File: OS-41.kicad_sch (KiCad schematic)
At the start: 65 parts, among them J1 Conn_02x03_Counter_Clockwise, J2 Conn_01x02_Pin, J3 Conn_01x02_Pin, J4 Conn_Coaxial, SW4 SW_Push, U1 BME280, U2 SI4432-B1-FMR, U3 MCP1640x-xCHY, U4 ATGM336H-5N31, U7 STM32F103C8Tx, Y1 32.768KHz 12.5pF, Y2 8MHz 12pF, Y3 30MHz 10pF

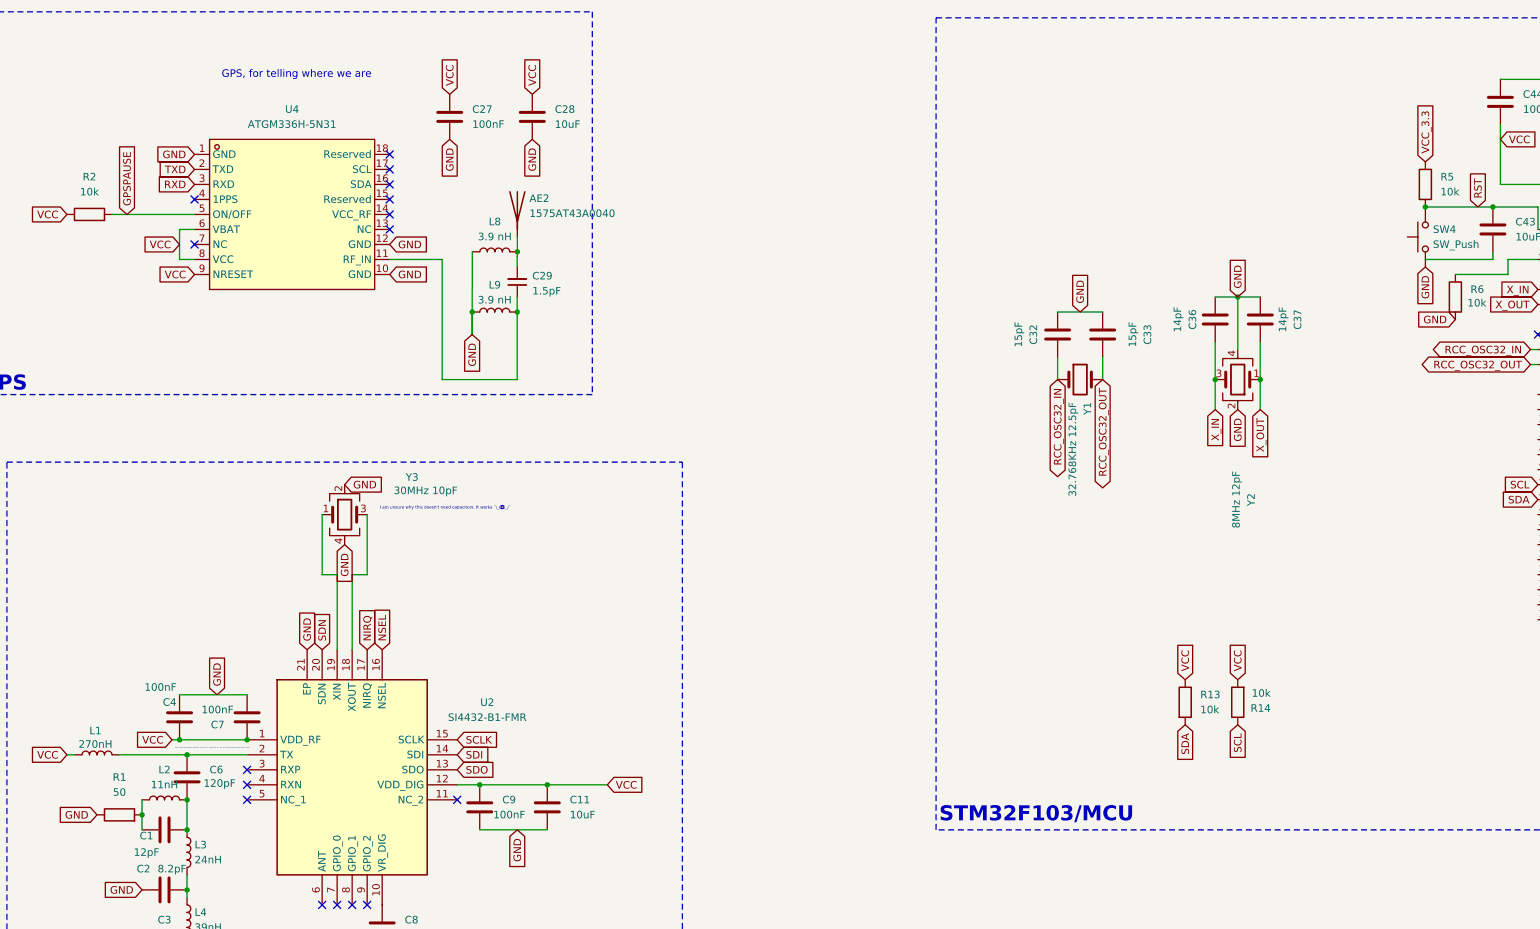
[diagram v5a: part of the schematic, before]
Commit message: More layout, no routing yet...
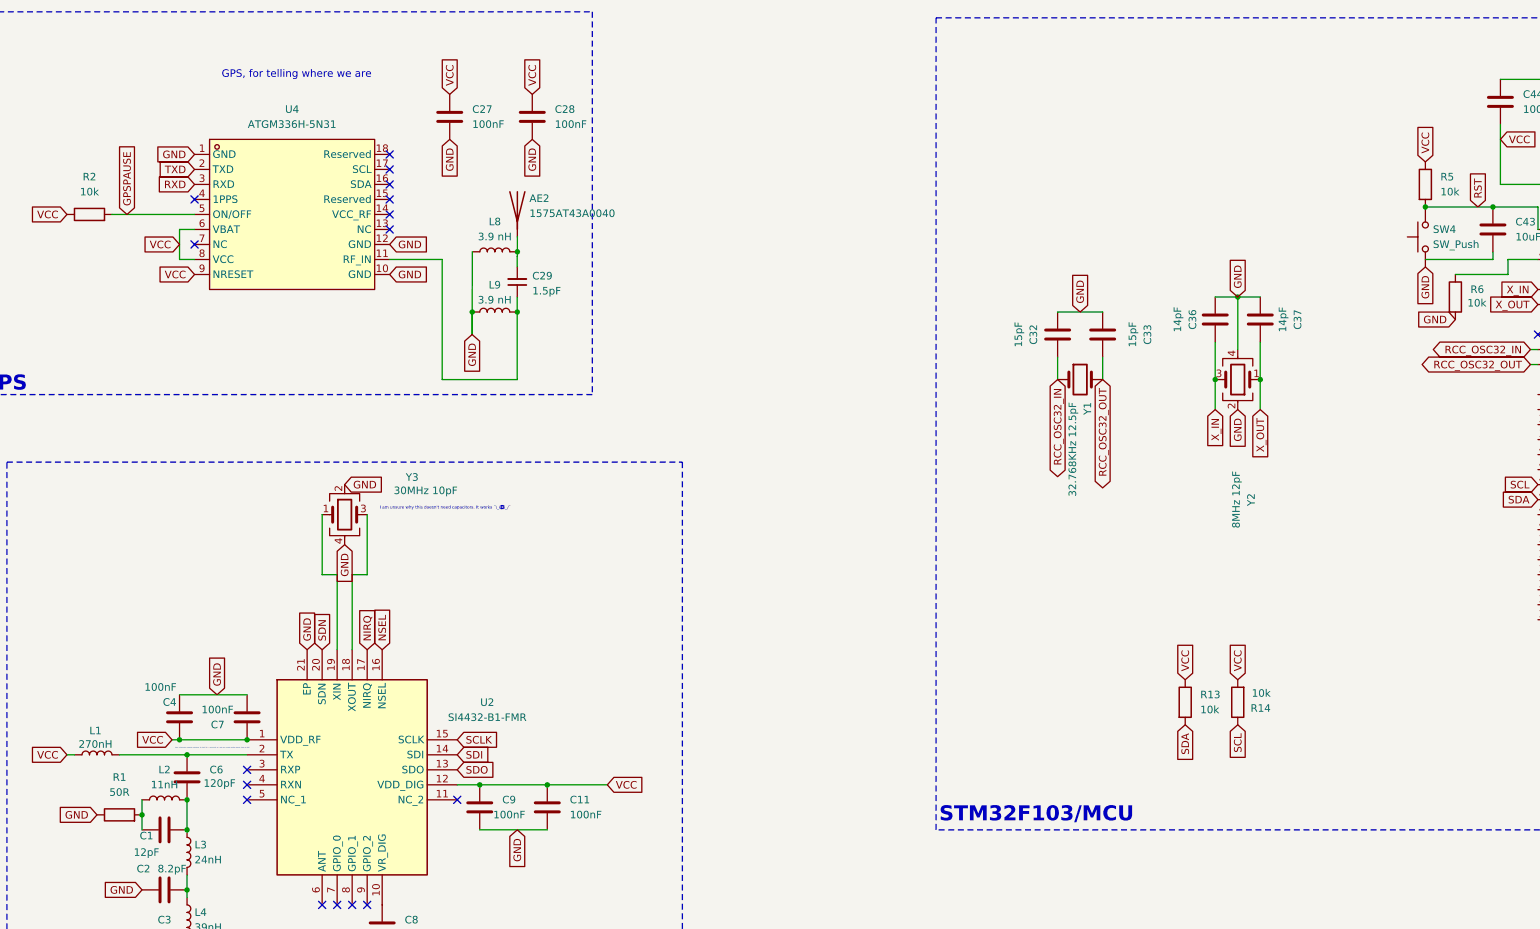
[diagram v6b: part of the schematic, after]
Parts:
- C11, C28: value 10uF -> 100nF
- R1: value 50 -> 50R
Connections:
- net VCC_3.3 is gone; now on net VCC: R5.1
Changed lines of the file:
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@@
 		)
 	)
-	(global_label "VCC_3.3"
+	(global_label "VCC"
 		(shape input)
 		(at 271.78 44.45 90)
@@
 		)
 		(property "Intersheetrefs" "${INTERSHEET_REFS}"
-			(at 271.78 33.8448 90)
+			(at 271.78 37.8362 90)
 			(effects
 				(font
@@
 			)
 		)
-		(property "Value" "50"
+		(property "Value" "50R"
 			(at 50.8 151.13 90)
 			(effects
@@
 			)
 		)
-		(property "Value" "10uF"
+		(property "Value" "100nF"
 			(at 124.46 38.0999 0)
 			(effects
@@
 			)
 		)
-		(property "Value" "10uF"
+		(property "Value" "100nF"
 			(at 127 154.9399 0)
 			(effects

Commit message: Start routing!
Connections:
- net GND: now also C43.2
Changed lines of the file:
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@@
+	(wire
+		(pts
+			(xy 283.21 60.96) (xy 271.78 60.96)
+		)
+		(stroke
+			(width 0)
+			(type default)
+		)
+	)
 	(wire
 		(pts
@@
 	(wire
 		(pts
-			(xy 271.78 60.96) (xy 283.21 60.96)
-		)
-		(stroke
-			(width 0)
-			(type default)
-		)
-	)
-	(wire
-		(pts
 			(xy 62.23 179.07) (xy 62.23 180.34)
 		)
@@
 		)
 		(stroke
+			(width 0)
+			(type default)
+		)
+	)
+	(wire
+		(pts
+			(xy 271.78 60.96) (xy 271.78 62.23)
+		)
+		(stroke

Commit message: Continue routing
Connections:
- net GPSPAUSE: now also U7.45 (PB8)
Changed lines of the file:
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@@
+		)
+	)
+	(global_label "GPSPAUSE"
+		(shape input)
+		(at 290.83 104.14 180)
+		(fields_autoplaced yes)
+		(effects
+			(font
+				(size 1.27 1.27)
+			)
+			(justify right)
+		)
+		(property "Intersheetrefs" "${INTERSHEET_REFS}"
+			(at 278.0477 104.14 0)
+			(effects
+				(font
+					(size 1.27 1.27)
+				)
+				(justify right)
+				(hide yes)
+			)
 		)
 	)
